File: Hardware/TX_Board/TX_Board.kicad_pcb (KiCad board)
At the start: 4 copper layers, 148 x 98.8 mm, 224 parts, among them IC1 GP2Y1+, IC10 QPA9122TR7, IC11 MAPS-010164-TR0500, IC12 QPA9122TR7, IC13 MAPS-010164-TR0500, IC14 QPA9122TR7, IC2 GP2Y1+, IC3 GP2Y1+, IC4 LT3041ADE#PBF, IC5 LT3099ADE#PBF, IC6 ADPL40502AUJZ-1.5-R7, IC7 MAPS-010164-TR0500, IC8 QPA9122TR7, IC9 MAPS-010164-TR0500, J1 Conn_Coaxial, J10 MM8030-2610RJ3, J11 MM8030-2610RJ3, J12 MM8030-2610RJ3, J13 MM8030-2610RJ3, J14 MM8030-2610RJ3, J15 Conn_Coaxial, J16 MM8030-2610RJ3, J17 MM8030-2610RJ3, J18 Conn_Coaxial, J19 MM8030-2610RJ3, J2 Conn_01x01_Pin, J20 MM8030-2610RJ3, J21 Conn_Coaxial, J22 MM8030-2610RJ3, J23 MM8030-2610RJ3, J24 Conn_Coaxial, J3 Conn_01x01_Pin, J4 Conn_01x01_Pin, J5 Conn_01x01_Pin, J6 Conn_02x12_Odd_Even, J7 Conn_01x03_Socket, J8 Conn_02x08_Odd_Even, J9 MM8030-2610RJ3, U1 SN74HCT138NSR

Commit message: more routing
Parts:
- moved J8 0.06 mm to (87.5, 53.9)
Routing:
- net ATTN_CLK: track 2.54 -> 75.0 mm
- net ATTN_SI: track 2.54 -> 74.6 mm
- net PS_SER_OUT: track 2.54 -> 65.1 mm
- net PS_CLK: track 2.54 -> 61.9 mm
- net PS_SER_IN: track 2.54 -> 61.0 mm
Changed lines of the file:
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@@
 	(footprint "Connector_PinHeader_2.54mm:PinHeader_2x08_P2.54mm_Vertical"
 		(layer "F.Cu")
-		(at 87.5 54 180)
+		(at 87.51 53.94 180)
 		(descr "Through hole straight pin header, 2x08, 2.54mm pitch, double rows")
 		(tags "Through hole pin header THT 2x08 2.54mm double row")
 		(property "Reference" "J8"
-			(at 1.27 -2.38 180)
+			(at 1.27 -2.38 0)
 			(layer "F.SilkS")
 			(effects
@@
 		)
 		(property "Value" "Conn_02x08_Odd_Even"
-			(at 1.27 20.16 180)
+			(at 1.27 20.16 0)
 			(layer "F.Fab")
 			(effects
@@
 		)
 		(property "Datasheet" "~"
-			(at 0 0 180)
+			(at 0 0 0)
 			(layer "F.Fab")
 			(hide yes)
@@
 		)
 		(property "Description" "Generic connector, double row, 02x08, odd/even pin numbering scheme (row 1 odd numbers, row 2 even numbers), script generated (kicad-library-utils/schlib/autogen/connector/)"
-			(at 0 0 180)
+			(at 0 0 0)
 			(layer "F.Fab")
 			(hide yes)
@@
 		)
 		(fp_text user "${REFERENCE}"
-			(at 1.27 8.89 270)
+			(at 1.27 8.89 90)
 			(layer "F.Fab")
 			(effects
@@
 		(fill no)
 		(layer "In1.Cu")
+		(net 48)
 	)
 	(gr_rect
@@
 	)
 	(segment
+		(start 167.12 35.18)
+		(end 174.24 35.18)
+		(width 0.2)
+		(layer "In2.Cu")
+		(net 64)
+	)
+	(segment
+		(start 174.24 35.18)
+		(end 174.4 35.34)
+		(width 0.2)
+		(layer "In2.Cu")
+		(net 64)
+	)
+	(segment
+		(start 125.281 40.371)
+		(end 161.929 40.371)
+		(width 0.2)
+		(layer "In2.Cu")
+		(net 64)
+	)
+	(segment
+		(start 174.4 35.34)
+		(end 174.4 35.975)
+		(width 0.2)
+		(layer "In2.Cu")
+		(net 64)
+	)
+	(segment
+		(start 120.66 35.75)
+		(end 125.281 40.371)
+		(width 0.2)
+		(layer "In2.Cu")
+		(net 64)
+	)
+	(segment
+		(start 161.929 40.371)
+		(end 167.12 35.18)
+		(width 0.2)
+		(layer "In2.Cu")
+		(net 64)
+	)
+	(segment
 		(start 123.2 33.21)
 		(end 123.2 35.75)
@@
 	)
 	(segment
+		(start 177.4 35.15)
+		(end 177.4 35.975)
+		(width 0.2)
+		(layer "In2.Cu")
+		(net 65)
+	)
+	(segment
+		(start 123.2 35.75)
+		(end 127.42 39.97)
+		(width 0.2)
+		(layer "In2.Cu")
+		(net 65)
+	)
+	(segment
+		(start 166.83 34.45)
+		(end 176.7 34.45)
+		(width 0.2)
+		(layer "In2.Cu")
+		(net 65)
+	)
+	(segment
+		(start 161.31 39.97)
+		(end 166.83 34.45)
+		(width 0.2)
+		(layer "In2.Cu")
+		(net 65)
+	)
+	(segment
+		(start 127.42 39.97)
+		(end 161.31 39.97)
+		(width 0.2)
+		(layer "In2.Cu")
+		(net 65)
+	)
+	(segment
+		(start 176.7 34.45)
+		(end 177.4 35.15)
+		(width 0.2)
+		(layer "In2.Cu")
+		(net 65)
+	)
+	(segment
 		(start 125.74 33.21)
 		(end 125.74 35.75)
@@
 	)
 	(segment
+		(start 181.85 33.97)
+		(end 166.53 33.97)
+		(width 0.2)
+		(layer "In2.Cu")
+		(net 66)
+	)
+	(segment
+		(start 129.44 39.45)
+		(end 125.74 35.75)
+		(width 0.2)
+		(layer "In2.Cu")
+		(net 66)
+	)
+	(segment
+		(start 183.4 35.975)
+		(end 183.4 35.52)
+		(width 0.2)
+		(layer "In2.Cu")
+		(net 66)
+	)
+	(segment
+		(start 166.53 33.97)
+		(end 161.05 39.45)
+		(width 0.2)
+		(layer "In2.Cu")
+		(net 66)
+	)
+	(segment
+		(start 161.05 39.45)
+		(end 129.44 39.45)
+		(width 0.2)
+		(layer "In2.Cu")
+		(net 66)
+	)
+	(segment
+		(start 183.4 35.52)
+		(end 181.85 33.97)
+		(width 0.2)
+		(layer "In2.Cu")
+		(net 66)
+	)
+	(segment
 		(start 204.48 91.01)
 		(end 197.6 91.01)
@@
 	)
 	(segment
+		(start 130.82 35.75)
+		(end 133.718 38.648)
+		(width 0.2)
+		(layer "In2.Cu")
+		(net 68)
+	)
+	(segment
+		(start 166.01 33.168)
+		(end 194.893 33.168)
+		(width 0.2)
+		(layer "In2.Cu")
+		(net 68)
+	)
+	(segment
+		(start 160.53 38.648)
+		(end 166.01 33.168)
+		(width 0.2)
+		(layer "In2.Cu")
+		(net 68)
+	)
+	(segment
+		(start 194.893 33.168)
+		(end 198.4 36.675)
+		(width 0.2)
+		(layer "In2.Cu")
+		(net 68)
+	)
+	(segment
+		(start 133.718 38.648)
+		(end 160.53 38.648)
+		(width 0.2)
+		(layer "In2.Cu")
+		(net 68)
+	)
+	(segment
 		(start 213.22 92.08)
 		(end 213.3 92)
@@
 	)
 	(segment
+		(start 192.294 33.569)
+		(end 195.4 36.675)
+		(width 0.2)
+		(layer "In2.Cu")
+		(net 70)
+	)
+	(segment
+		(start 131.579 39.049)
+		(end 160.8839 39.049)
+		(width 0.2)
+		(layer "In2.Cu")
+		(net 70)
+	)
+	(segment
+		(start 160.8839 39.049)
+		(end 166.3639 33.569)
+		(width 0.2)
+		(layer "In2.Cu")
+		(net 70)
+	)
+	(segment
+		(start 128.28 35.75)
+		(end 131.579 39.049)
+		(width 0.2)
+		(layer "In2.Cu")
+		(net 70)
+	)
+	(segment
+		(start 166.3639 33.569)
+		(end 192.294 33.569)
+		(width 0.2)
+		(layer "In2.Cu")
+		(net 70)
+	)
+	(segment
 		(start 215.32 88.095)
 		(end 214.85 87.625)
@@
 		(priority 5)
 		(connect_pads
-			(clearance 0.2)
+			(clearance 0.5)
 		)
 		(min_thickness 0.25)

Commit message: more routing
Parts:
- moved J8 0.17 mm to (87.5, 53.8)
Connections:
- J8 pad 1: PS_LE_1 -> ATTN_LE_4
- J8 pad 10: PS_LE_3 -> PS_LE_4
- J8 pad 11: ATTN_LE_3 -> PS_LE_3
- J8 pad 12: ATTN_LE_3 -> PS_LE_3
- J8 pad 13: PS_LE_4 -> PS_LE_2
- J8 pad 14: PS_LE_4 -> PS_LE_2
- J8 pad 15: ATTN_LE_4 -> PS_LE_1
- J8 pad 16: ATTN_LE_4 -> PS_LE_1
- J8 pad 2: PS_LE_1 -> ATTN_LE_4
- J8 pad 3: ATTN_LE_1 -> ATTN_LE_3
- J8 pad 4: ATTN_LE_1 -> ATTN_LE_3
- J8 pad 5: PS_LE_2 -> ATTN_LE_2
- J8 pad 6: PS_LE_2 -> ATTN_LE_2
- J8 pad 7: ATTN_LE_2 -> ATTN_LE_1
- J8 pad 8: ATTN_LE_2 -> ATTN_LE_1
- J8 pad 9: PS_LE_3 -> PS_LE_4
- R10 pad 2: ATTN_LE_3 -> PS_LE_3
- R11 pad 2: PS_LE_4 -> PS_LE_2
- R3 pad 1: ATTN_LE_4 -> PS_LE_1
- R5 pad 2: PS_LE_1 -> ATTN_LE_4
- R6 pad 2: ATTN_LE_1 -> ATTN_LE_3
- R7 pad 2: PS_LE_2 -> ATTN_LE_2
- R8 pad 2: ATTN_LE_2 -> ATTN_LE_1
- R9 pad 2: PS_LE_3 -> PS_LE_4
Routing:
- net ATTN_LE_1: track 9.87 -> 229.0 mm
- net ATTN_LE_2: track 8.98 -> 204.9 mm
- net PS_LE_1: track 10.3 -> 198.3 mm
- net ATTN_LE_3: track 9.33 -> 180.6 mm
- net PS_LE_2: track 9.43 -> 170.4 mm
- net PS_LE_3: track 8.89 -> 145.8 mm
- net ATTN_LE_4: track 28.1 -> 157.4 mm
- net PS_LE_4: track 9.77 -> 121.4 mm
- net ATTN_SI: track 74.6 -> 146.2 mm
- net ATTN_CLK: track 75.0 -> 146.7 mm
- net PS_SER_OUT: track 65.1 -> 136.5 mm
- net PS_SER_IN: track 61.0 -> 132.4 mm
- net PS_CLK: track 61.9 -> 133.0 mm
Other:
- board text added: "${REFERENCE}"

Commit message: routing + odb++ export
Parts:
- moved R13 1.52 mm to (95.0, 105.7), turned to 180 degrees
- moved R16 0.89 mm to (94.3, 105.0)
- moved C12 0.52 mm to (95.6, 118.8)
- moved R12 0.50 mm to (93.7, 103.6)
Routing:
- net V_PD: track 0.00 -> 216.1 mm
- net VEE: track 18.4 -> 217.3 mm
- net VCC: track 76.1 -> 175.2 mm, vias 20 -> 26
- net PS_LE_1: track 198.3 -> 245.5 mm
- net PS_LE_4: track 121.4 -> 154.6 mm
- net PS_LE_2: track 170.4 -> 202.9 mm
- net PS_LE_3: track 145.8 -> 177.7 mm
- net ATTN_CLK: track 146.7 -> 122.4 mm
- net ATTN_LE_4: track 157.4 -> 174.2 mm
- net ATTN_LE_1: track 229.0 -> 244.1 mm
- net ATTN_LE_2: track 204.9 -> 219.8 mm
- net ATTN_LE_3: track 180.6 -> 194.2 mm
- net GND: track 0.00 -> 13.7 mm, vias 4 -> 129
- net +VDC: track 0.00 -> 11.1 mm
- net Net-(IC5-PGFB): track 0.00 -> 9.99 mm
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- added copper zone on B.Cu, net VCC

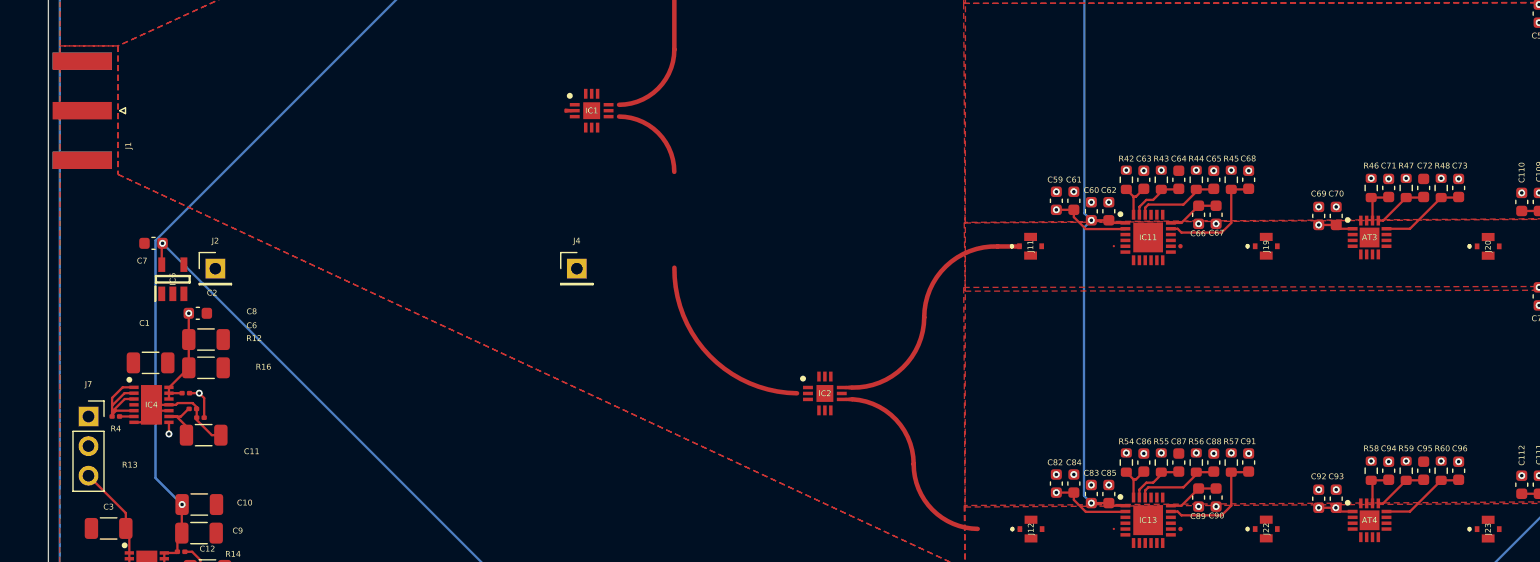
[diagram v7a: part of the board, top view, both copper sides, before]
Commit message: updated DRC for OSHpark
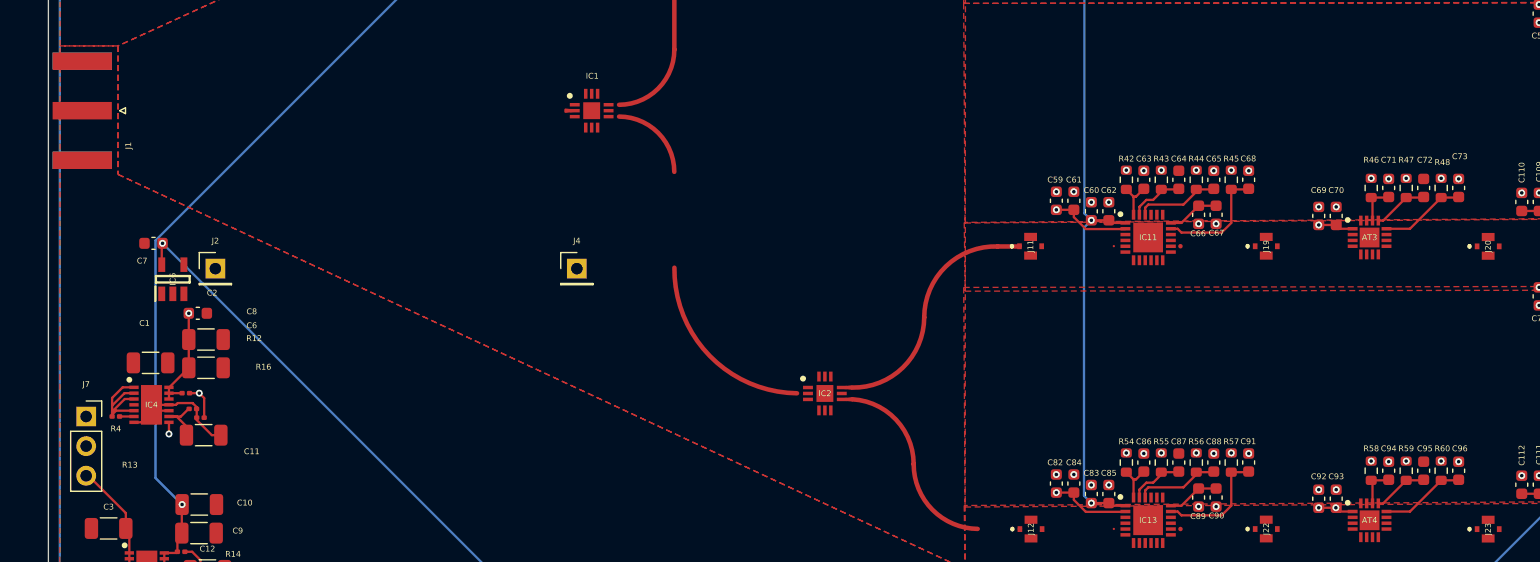
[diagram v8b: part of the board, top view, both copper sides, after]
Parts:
- moved J7 0.20 mm to (85.2, 105.6)
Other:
- rule pad_to_mask_clearance: 0 -> 0.0508
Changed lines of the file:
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@@
 			(dielectric_constraints no)
 		)
-		(pad_to_mask_clearance 0)
+		(pad_to_mask_clearance 0.0508)
 		(allow_soldermask_bridges_in_footprints no)
 		(tenting front back)
@@
 		(tags "resistor")
 		(property "Reference" "R46"
-			(at -1.9 0 0)
+			(at -2.4 0 0)
 			(layer "F.SilkS")
 			(effects
@@
 		(tags "capacitor")
 		(property "Reference" "C72"
-			(at 1.9 0.1 180)
+			(at 2.4 0.1 180)
 			(layer "F.SilkS")
 			(effects
@@
 		(tags "capacitor")
 		(property "Reference" "C71"
-			(at 1.9 0 0)
+			(at 2.4 0 0)
 			(layer "F.SilkS")
 			(effects
@@
 	(footprint "Connector_PinSocket_2.54mm:PinSocket_1x03_P2.54mm_Vertical"
 		(layer "F.Cu")
-		(at 85.4 105.6)
+		(at 85.2 105.6)
 		(descr "Through hole straight socket strip, 1x03, 2.54mm pitch, single row (from Kicad 4.0.7), script generated")
 		(tags "Through hole socket strip THT 1x03 2.54mm single row")
@@
 		(tags "capacitor")
 		(property "Reference" "C73"
-			(at -1.9 -0.1 0)
+			(at -2.7 -0.1 0)
 			(layer "F.SilkS")
 			(effects
@@
 		(tags "capacitor")
 		(property "Reference" "C70"
-			(at 1.9 0 180)
+			(at 2.2 0 180)
 			(layer "F.SilkS")
 			(effects
@@
 		(tags "capacitor")
 		(property "Reference" "C69"
-			(at 1.9 0 180)
+			(at 2.2 0 180)
 			(layer "F.SilkS")
 			(effects
@@
 		(tags "resistor")
 		(property "Reference" "R47"
-			(at 1.9 0 180)
+			(at 2.4 0 180)
 			(layer "F.SilkS")
 			(effects
@@
 		(tags "resistor")
 		(property "Reference" "R48"
-			(at 1.9 0.1 180)
+			(at 2.2 0.1 180)
 			(layer "F.SilkS")
 			(effects
@@
 		(tags "Integrated Circuit")
 		(property "Reference" "IC1"
-			(at 0 0 0)
+			(at 0.05 -2.975 0)
 			(layer "F.SilkS")
 			(effects
 				(font
 					(size 0.5 0.5)
-					(thickness 0.254)
+					(thickness 0.125)
 				)
 			)
@@
 		)
 		(fp_text user "${REFERENCE}"
-			(at 0 0 0)
+			(at 0.05 -2.975 0)
 			(layer "F.Fab")
 			(effects
@@
 	)
 	(segment
-		(start 106.2814 47.605)
-		(end 105.395 47.605)
+		(start 104.708701 48.291299)
+		(end 104.708701 50.8911)
 		(width 0.2)
 		(layer "F.Cu")
@@
 	)
 	(segment
-		(start 118.12 41.043264)
-		(end 118.12 35.75)
+		(start 104.708701 50.8911)
+		(end 104.943601 51.126)
 		(width 0.2)
 		(layer "F.Cu")
@@
 	)
 	(segment
-		(start 108.037264 51.126)
-		(end 118.12 41.043264)
+		(start 106.2814 47.605)
+		(end 105.395 47.605)
 		(width 0.2)
 		(layer "F.Cu")
@@
 	)
 	(segment
-		(start 105.395 47.605)
-		(end 104.708701 48.291299)
+		(start 118.12 41.043264)
+		(end 118.12 35.75)
 		(width 0.2)
 		(layer "F.Cu")
@@
 	)
 	(segment
-		(start 104.708701 50.8911)
-		(end 104.943601 51.126)
+		(start 104.943601 51.126)
+		(end 108.037264 51.126)
 		(width 0.2)
 		(layer "F.Cu")
@@
 	)
 	(segment
-		(start 104.708701 48.291299)
-		(end 104.708701 50.8911)
+		(start 108.037264 51.126)
+		(end 118.12 41.043264)
 		(width 0.2)
 		(layer "F.Cu")
@@
 	)
 	(segment
-		(start 118.12 33.21)
-		(end 118.12 35.75)
+		(start 105.395 47.605)
+		(end 104.708701 48.291299)
 		(width 0.2)
 		(layer "F.Cu")
@@
 	)
 	(segment
-		(start 104.943601 51.126)
-		(end 108.037264 51.126)
+		(start 118.12 33.21)
+		(end 118.12 35.75)
 		(width 0.2)
 		(layer "F.Cu")
